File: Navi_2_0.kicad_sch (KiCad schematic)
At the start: 116 parts, among them J1 USB_B_Micro, J10 BAT-, J2 Conn_01x24_Male, J23 Conn_01x06_Male, J27 Micro_SD_Card_Det, J8 SELECT, J9 BAT+, Q1 DMG2301L-7, Q2 Q_NMOS_GSD, Q3 DMG2301L-7, Q6 DMG2301L-7, SW1 SW_Push, SW2 SW_Push, SW3 WKUP, U1 MT3420C, U2 MT3420C, U3 ESP32-WROOM-32, U4 CH330N, U5 L96-M33, U6 LSM6DS3, U7 TCN75-3.3

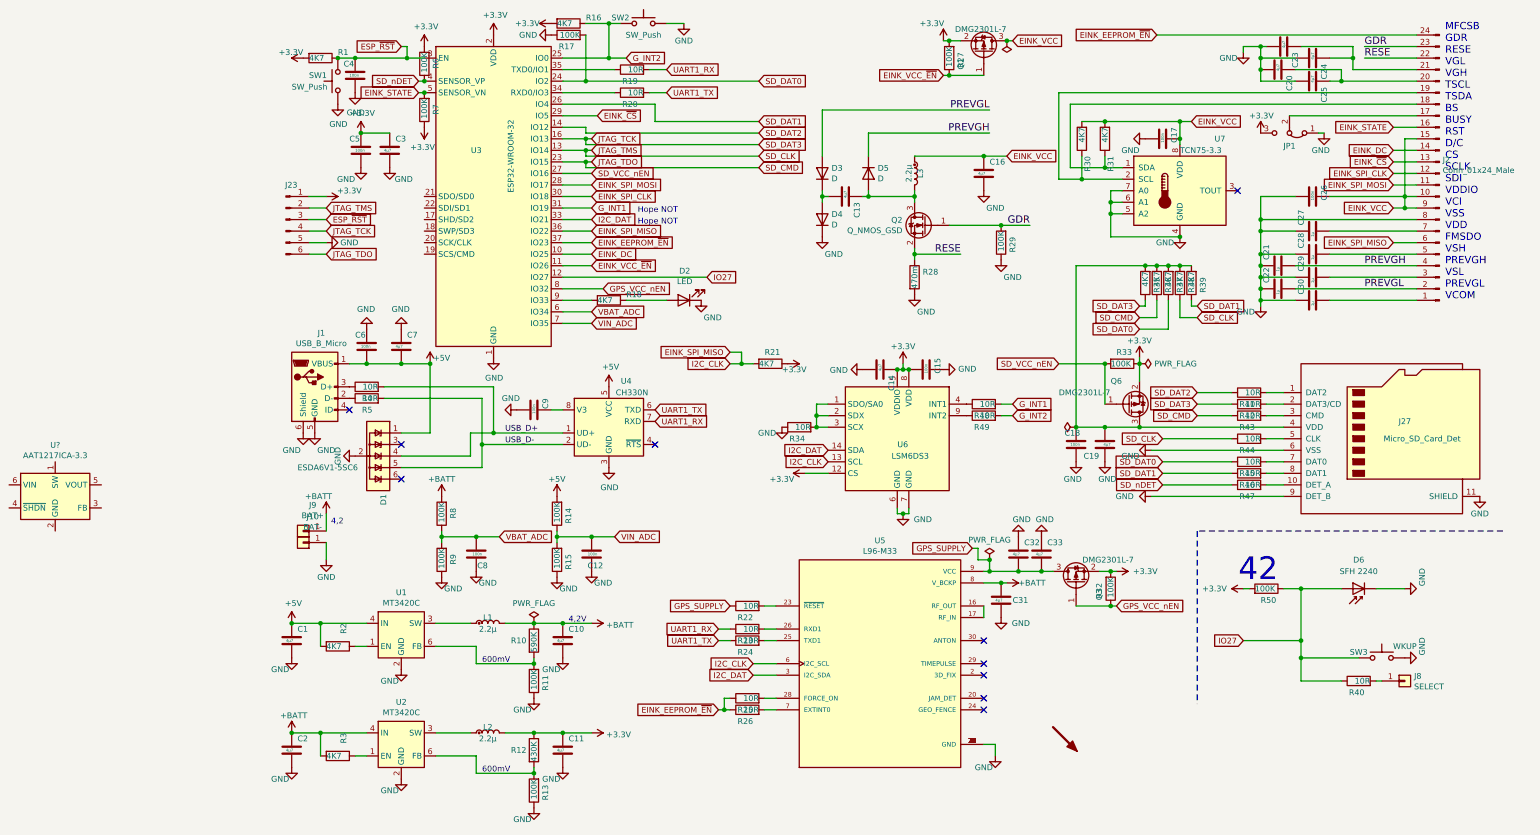
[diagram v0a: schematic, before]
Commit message: #4 Widerstand schaltbar gemacht
Der Widerstand wurde per MOSFET schaltbar gemacht, da sonst kein Updaten Per UART möglich war
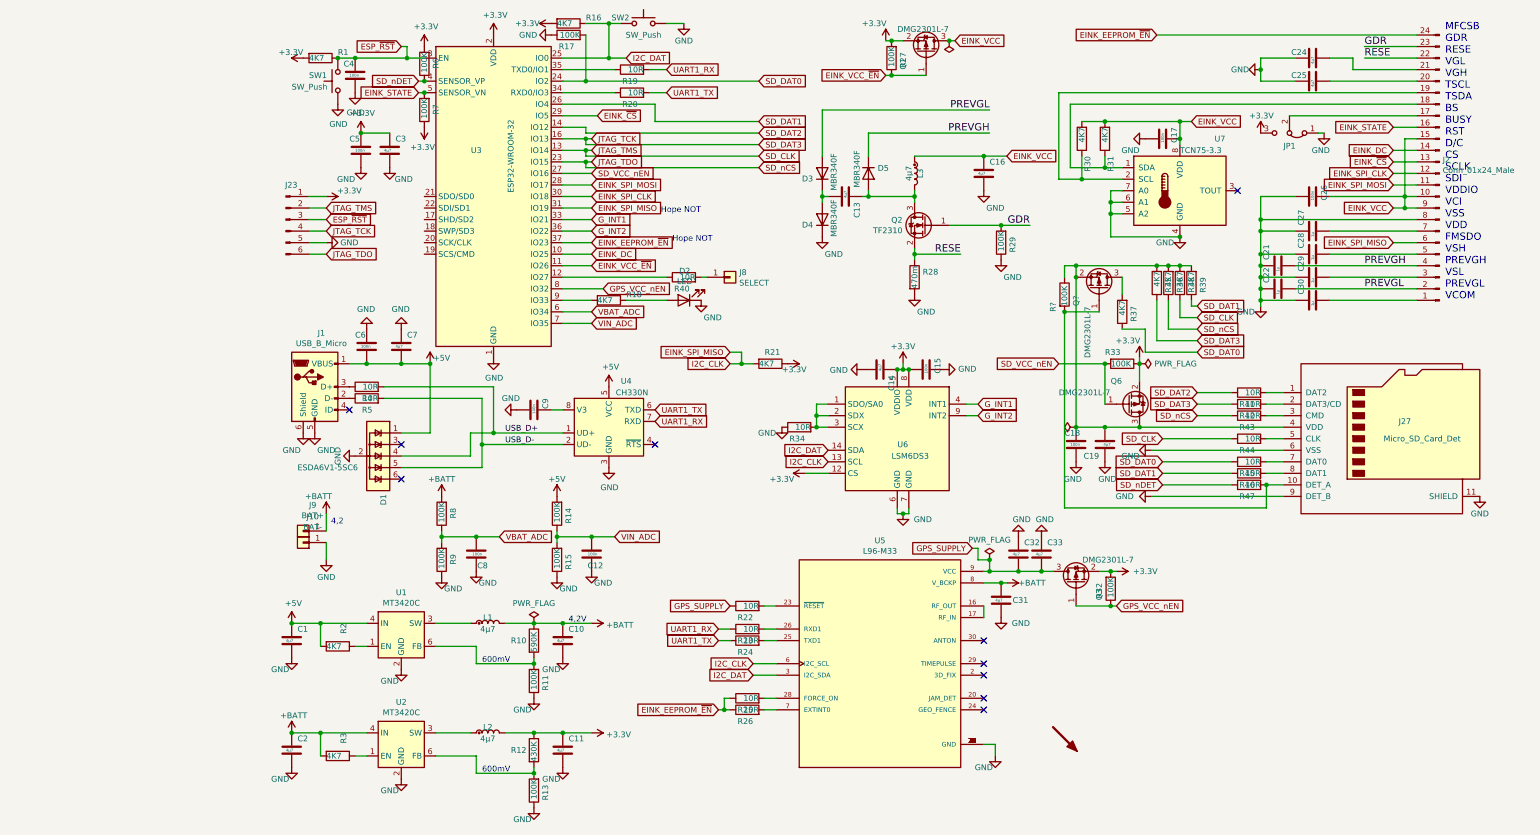
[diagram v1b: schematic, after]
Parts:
- removed C20, C23: 4µ7, Capacitor_SMD:C_0603_1608Metric, symbol Device:C
- removed D6: SFH 2240, Diode_SMD:D_SMB, symbol Device:D_Photo
- removed R48, R49: 10R, Resistor_SMD:R_0603_1608Metric, symbol Device:R
- removed R50: 100K, Resistor_SMD:R_0603_1608Metric, symbol Device:R
- removed SW3: WKUP, Button_Switch_SMD:SW_DIP_SPSTx01_Slide_6.7x4.1mm_W6.73mm_P2.54mm_LowProfile_JPin, symbol Switch:SW_Push
- removed U?: AAT1217ICA-3.3, Package_TO_SOT_SMD:TSOT-23-6, symbol Regulator_Switching:AAT1217ICA-3.3
- added Q?: DMG2301L-7, Package_TO_SOT_SMD:TSOT-23, symbol Device:Q_PMOS_GSD
- added R?: 100K, Resistor_SMD:R_0603_1608Metric, symbol Device:R
- C13, C24, C25: footprint Capacitor_SMD:C_0603_1608Metric -> Capacitor_SMD:C_1206_3216Metric; LCSC C307468 -> C513768
- D3, D4, D5: value D -> MBR340F; LCSC C383230 -> C475721
- J23: footprint Connector:Tag-Connect_TC2030-IDC-NL_2x03_P1.27mm_Vertical -> Connector:Tag-Connect_TC2030-IDC-FP_2x03_P1.27mm_Vertical
- L1, L2, L3: value 2.2µ -> 4µ7; LCSC C439320 -> C88536
- Q2: value Q_NMOS_GSD -> TF2310; LCSC C212304 -> C436854
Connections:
- net EINK_SPI_MISO: now also U3.31 (IO19); no longer U3.36 (IO22)
- net GND: now also C24.1, C25.1; no longer C24.2, C25.2
- net G_INT1: now also U3.33 (IO21), U6.4 (INT1); no longer U3.31 (IO19)
- net G_INT2: now also U3.36 (IO22), U6.9 (INT2); no longer R16.1, SW2.2, U3.25 (IO0)
- net I2C_DAT: now also R16.1, SW2.2, U3.25 (IO0); no longer U3.33 (IO21)
- net at C18.1, C19.2, J27.4 (VDD)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: now also Q?.2 (S), R?.1; no longer R37.2
- net at J27.10 (DET_A), R47.2: now also Q?.1 (G), R?.2
- net at J2.20 (Pin_20): now also C25.2; no longer C25.1
- net at J2.21 (Pin_21): now also C24.2; no longer C24.1
- net IO27: no longer names the net of R40.1, U3.12 (IO27)
- new net: Q?.3 (D), R37.2
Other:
- note removed: "42"
- moved on the sheet: J8, Q1, R27, R35, R36, R37, R40
